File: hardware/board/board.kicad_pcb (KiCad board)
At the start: 4 copper layers, 300 x 120 mm, 235 parts, among them J201 LineOut, J202 Headphone, J203 LineIn, J301 MidiIn, J302 MidiOut, J501 USB_B_Micro, J502 USB_C_Receptacle_PowerOnly_6P, P501 USB_C_Plug_USB2.0, SW401 SW_Push, SW402 SW_Push, SW403 SW_Push, SW404 SW_Push, SW405 SW_Push, SW406 SW_Push, SW407 SW_Push, SW408 SW_Push, SW409 SW_Push, SW410 SW_Push, SW411 SW_Push, SW412 SW_Push, SW413 SW_Push, SW414 SW_Push, SW415 SW_Push, SW416 SW_Push, SW417 SW_Push, SW418 SW_Push, SW419 SW_Push, SW420 SW_Push, SW421 SW_Push, SW422 SW_Push, SW423 SW_Push, SW424 SW_Push, SW425 SW_Push, SW426 SW_Push, SW427 SW_Push, SW428 SW_Push, SW429 SW_Push, SW430 SW_Push, SW431 SW_Push, SW432 SW_Push, SW433 SW_Push, SW434 SW_Push, SW435 SW_Push, SW436 SW_Push, SW437 SW_Push, SW438 SW_Push, SW439 SW_Push, SW440 SW_Push, SW441 SW_Push, U101 Oled, U201 QFN40P700X700X80-57N, U202 TPS7A20xxxDBV, U301 RP2350_80QFN, U302 CNK_THB001P, U303 TLP2310, U304 74AHC1G125DCKR, U501 AP22653W6, U502 FSUSB42MX, U503 TPS259531DSGR, Y201 12.288MHz, Y301 ABM8-272-T3

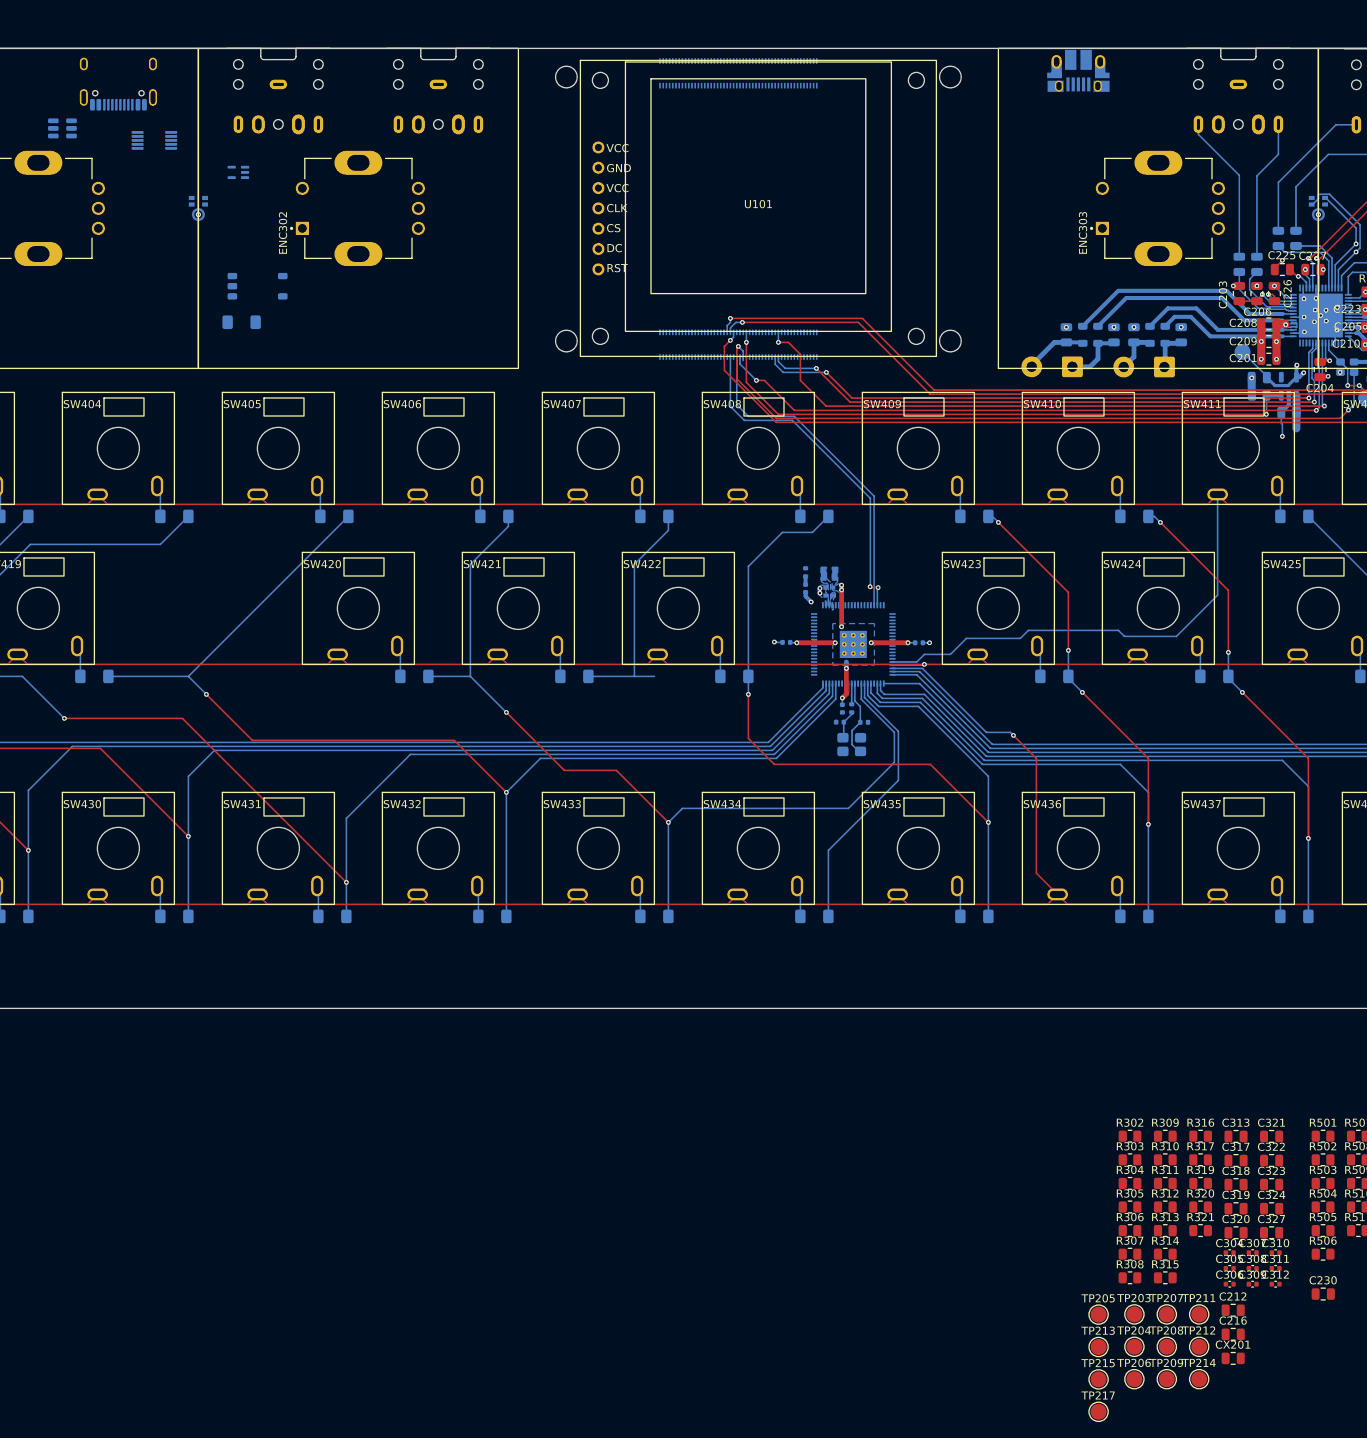
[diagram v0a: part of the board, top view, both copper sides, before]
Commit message: caps for 2350
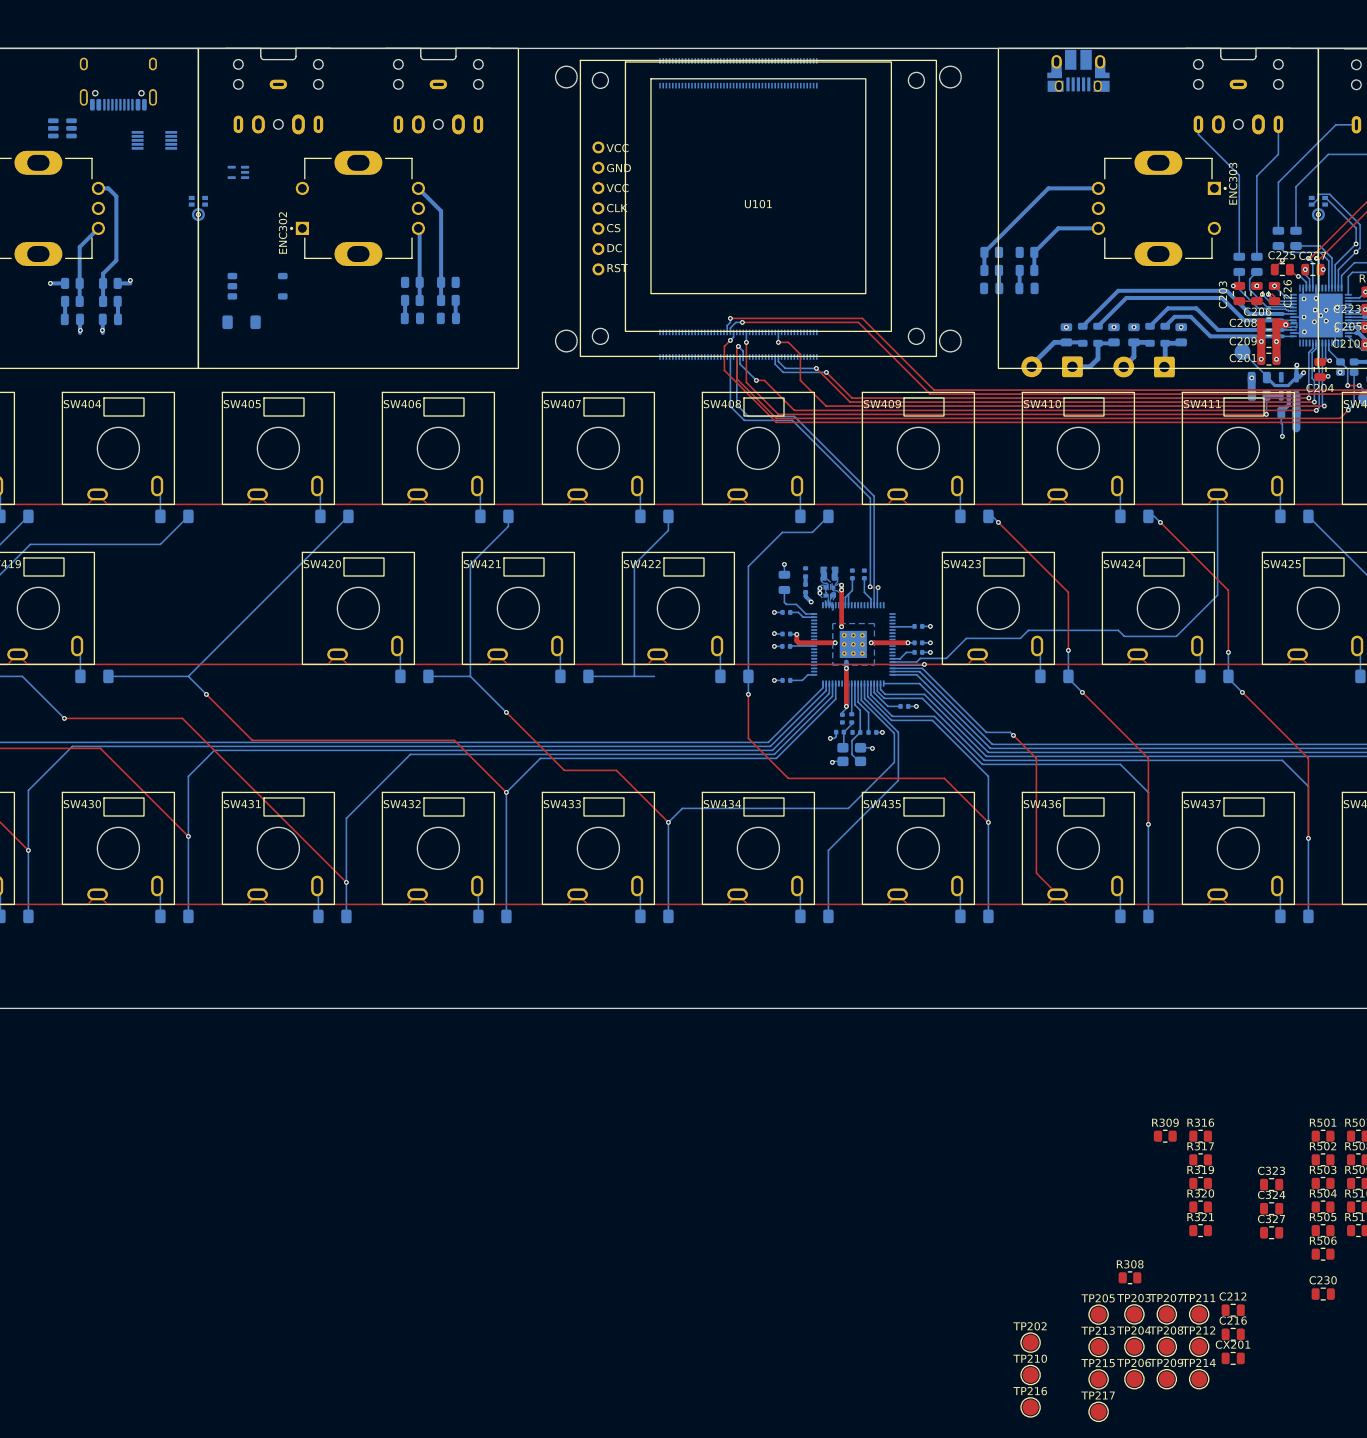
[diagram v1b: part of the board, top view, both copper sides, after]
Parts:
- added TP202: SPKLP, TestPoint:TestPoint_Pad_D2.0mm, F.Cu at (251.5, 245.3)
- added TP210: SPKRP, TestPoint:TestPoint_Pad_D2.0mm, F.Cu at (251.5, 249.3)
- added TP216: SPKRN, TestPoint:TestPoint_Pad_D2.0mm, F.Cu at (251.5, 253.4)
- C304, C305, C306, C307, C308, C309, C310, C311, C312, C313, C317, C318, C319, C320, C321, C322, R302, R303, R304, R305, R306, R307, R310, R311, R312, R313, R314, R315: moved to B.Cu
- U201: value QFN40P700X700X80-57N -> MAX98089ETN_T
- U302: value CNK_THB001P -> THB001P
- moved C317 179.5 mm to (131.8, 117.4)
- moved C318 177.5 mm to (136.5, 117.4), turned to 180 degrees
- moved R310 173.7 mm to (131.8, 115.1), turned to 180 degrees
- moved R311 171.9 mm to (136.5, 115.1)
- moved R302 169.8 mm to (131.8, 112.9)
- moved R303 168.1 mm to (136.5, 112.9), turned to 180 degrees
- moved C319 151.6 mm to (174.2, 117.2)
- moved C320 150.9 mm to (178.8, 117.2), turned to 180 degrees
- moved R312 147.3 mm to (174.2, 115.0), turned to 180 degrees
- moved R313 146.8 mm to (178.8, 115.0)
- moved R304 144.0 mm to (174.2, 112.8)
- moved R305 143.6 mm to (178.8, 112.8), turned to 180 degrees
- moved R315 127.1 mm to (251.1, 111.2), turned to 180 degrees
- moved R307 125.9 mm to (251.1, 109.0)
- moved R314 124.9 mm to (246.7, 111.2)
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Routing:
- net +3V3: track 12.1 -> 57.4 mm, vias 4 -> 6
- net Net-(ENC303-PadA): track 0.00 -> 19.8 mm
- net Net-(ENC301-PadB): track 0.00 -> 16.5 mm
- net GND: track 94.9 -> 111.1 mm, vias 38 -> 51
- net Net-(ENC302-PadB): track 0.00 -> 15.2 mm
- net Net-(ENC303-PadB): track 0.00 -> 11.5 mm
- net Net-(ENC301-PadA): track 0.00 -> 10.1 mm
- net Net-(ENC302-PadA): track 0.00 -> 9.07 mm
- net +1V1: track 28.5 -> 32.2 mm
- net /mcu/ENC1_B: track 0.00 -> 2.32 mm
- net /mcu/ENC3_A: track 0.00 -> 2.27 mm
- net /mcu/ENC3_B: track 0.00 -> 2.27 mm
- net /mcu/ENC2_B: track 0.00 -> 2.27 mm
- net /mcu/ENC2_A: track 0.00 -> 2.27 mm
- net /mcu/ENC1_A: track 0.00 -> 2.27 mm
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
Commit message: big routing board
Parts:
- added J101: UART, Connector_PinHeader_1.27mm:PinHeader_1x03_P1.27mm_Vertical, F.Cu at (234.6, 228.9)
- added J102: CM4_DEBUG, Connector_PinHeader_1.27mm:PinHeader_1x03_P1.27mm_Vertical, F.Cu at (238.7, 228.9)
- added J103: DEBUG_PORT, Connector_PinHeader_1.27mm:PinHeader_1x03_P1.27mm_Vertical, F.Cu at (242.9, 228.9)
- C323, C324, C327, R308, R309, R316, R317, R319, R320, R321: moved to B.Cu
- moved C327 180.3 mm to (157.5, 100.8), turned to -90 degrees
- moved R321 179.7 mm to (152.8, 97.5), turned to 180 degrees
- moved R320 174.9 mm to (156.8, 97.5), turned to 180 degrees
- moved R319 157.6 mm to (178.8, 98.8), turned to -90 degrees
- moved R308 133.2 mm to (314.0, 113.8), turned to 180 degrees
- moved R309 117.0 mm to (318.5, 113.8)
- moved C324 116.3 mm to (318.6, 118.2)
- moved R317 115.8 mm to (318.5, 116.0), turned to 180 degrees
- moved C323 112.0 mm to (314.0, 118.2), turned to 180 degrees
- moved R316 111.4 mm to (314.0, 116.0)
- moved U502 111.2 mm to (253.2, 92.8)
- moved D301 36.3 mm to (183.5, 98.2), turned to 0 degrees
- moved U303 30.0 mm to (183.5, 104.2), turned to -90 degrees
- moved U304 2.34 mm to (154.2, 100.7), turned to 90 degrees
- moved R302 0.15 mm to (131.8, 113.0), turned to 180 degrees
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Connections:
- U301 pad 3: /mcu/ENC1_A -> /mcu/ENC3_A
- U301 pad 4: /mcu/ENC1_B -> /mcu/ENC3_B
- U301 pad 42: unconnected-(U301-GPIO33-Pad42) -> /mcu/ENC1_SW
- U301 pad 43: /mcu/ENC3_A -> /mcu/ENC2_SW
- U301 pad 44: /mcu/ENC3_B -> /mcu/ENC1_A
- U301 pad 45: /mcu/ENC4_A -> /mcu/ENC1_B
- U301 pad 46: /mcu/ENC4_B -> /mcu/ENC2_A
- U301 pad 47: /mcu/ENC3_SW -> /mcu/ENC2_B
- U301 pad 48: /mcu/ENC4_SW -> unconnected-(U301-GPIO39-Pad48)
- U301 pad 52: unconnected-(U301-GPIO41_ADC1-Pad52) -> /mcu/JOYSTICK_X
- U301 pad 53: unconnected-(U301-GPIO42_ADC2-Pad53) -> /mcu/JOYSTICK_Y
- U301 pad 56: /mcu/JOYSTICK_X -> unconnected-(U301-GPIO45_ADC5-Pad56)
- U301 pad 57: /mcu/JOYSTICK_Y -> unconnected-(U301-GPIO46_ADC6-Pad57)
- U301 pad 6: /mcu/ENC2_A -> /mcu/ENC4_A
- U301 pad 7: /mcu/ENC2_B -> /mcu/ENC4_B
- U301 pad 79: /mcu/ENC1_SW -> /mcu/ENC3_SW
- U301 pad 80: /mcu/ENC2_SW -> /mcu/ENC4_SW
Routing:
- net /audio/DIGMICCLK: track 17.5 -> 174.0 mm, vias 1 -> 3
- net /audio/DIGMICDATA: track 14.0 -> 167.7 mm, vias 1 -> 3
- net /mcu/ENC1_SW: track 0.00 -> 140.4 mm
- net /mcu/ENC1_A: track 2.27 -> 115.4 mm
- net /mcu/ENC1_B: track 2.32 -> 111.8 mm
- net /mcu/ENC2_SW: track 0.00 -> 106.3 mm, vias 0 -> 2
- net /mcu/ENC4_B: track 0.00 -> 102.9 mm
- net /mcu/ENC4_A: track 0.00 -> 101.0 mm
- net /mcu/MIDI_RX: track 0.00 -> 93.4 mm
- net /mcu/ENC2_A: track 2.27 -> 75.5 mm
- net /mcu/ENC2_B: track 2.27 -> 72.1 mm
- net /mcu/ENC3_B: track 2.27 -> 53.6 mm
- net /mcu/ENC3_A: track 2.27 -> 51.5 mm
- net /mcu/MIDI_TX: track 0.00 -> 42.5 mm
- net /mcu/matrix_C6: track 64.5 -> 95.3 mm, vias 0 -> 4
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
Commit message: some big tim routing
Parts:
- C221: value 1uF -> 47pF
- C222: value 470pF -> 1uF
- C223: value 1uF -> 470pF
- C224: value 2.2uF -> 1uF
- C225: value 1uF -> 2.2uF
- C230: value 47pF -> 1uF
- C501, C502, C503, C504, C505, R501, R502, R503, R504, R505, R506, R507: moved to B.Cu
- J502: value USB_C_Receptacle_PowerOnly_6P -> USB_C_Receptacle_PowerOnly_24P
- R508: value 390k -> 5.1k; moved to B.Cu
- R509: value 681 @ 1% -> 5.1k; moved to B.Cu
- R510: value 5.1k -> 390k; moved to B.Cu
- R511: value 5.1k -> 681 @ 1%; moved to B.Cu
- moved C501 292.4 mm to (75.4, 28.7), turned to 180 degrees
- moved C502 292.4 mm to (75.4, 31.7), turned to 180 degrees
- moved R502 279.2 mm to (84.2, 31.6), turned to 180 degrees
- moved R504 279.2 mm to (84.2, 37.5), turned to 180 degrees
- moved C505 228.7 mm to (111.2, 98.0), turned to -90 degrees
- moved R510 226.0 mm to (110.8, 94.0), turned to 90 degrees
- moved R511 222.0 mm to (112.5, 101.2), turned to 180 degrees
- moved C504 220.6 mm to (116.8, 101.2)
- moved C503 220.3 mm to (117.2, 98.0), turned to -90 degrees
- moved R509 219.4 mm to (116.8, 94.0), turned to -90 degrees
- moved R507 219.0 mm to (113.0, 94.0), turned to -90 degrees
- moved R506 218.9 mm to (112.5, 103.5)
- moved R508 215.9 mm to (119.0, 94.0), turned to -90 degrees
- moved R503 197.2 mm to (139.8, 95.5), turned to 180 degrees
- moved R501 194.8 mm to (139.8, 93.2), turned to 180 degrees
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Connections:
- C221 pad 1: Net-(C221-Pad1) -> unconnected-(C221-Pad1)
- C221 pad 2: Net-(U201-INA2/EXTMICN) -> unconnected-(C221-Pad2)
- C222 pad 2: GND -> Net-(U201-INA2/EXTMICN)
- C223 pad 1: Net-(U201-REG) -> Net-(C223-Pad1)
- C224 pad 1: Net-(U201-REF) -> Net-(U201-REG)
- C225 pad 1: Net-(U201-HPVSS) -> Net-(U201-REF)
- C226 pad 1: /audio/C1N -> Net-(U201-HPVSS)
- C226 pad 2: /audio/C1P -> GND
- C227 pad 1: Net-(U201-HPVDD) -> /audio/C1N
- C227 pad 2: GND -> /audio/C1P
- C228 pad 1: +3V3 -> Net-(U201-HPVDD)
- C229 pad 1: +1V8 -> +3V3
- C230 pad 1: unconnected-(C230-Pad1) -> +1V8
- C230 pad 2: unconnected-(C230-Pad2) -> GND
- FB205 pad 2: Net-(C222-Pad1) -> Net-(C223-Pad1)
- J203 pad R: Net-(C221-Pad1) -> Net-(C222-Pad1)
- J502 pad A1: (no net) -> GND
- J502 pad A4: (no net) -> Net-(C503-Pad1)
- J502 pad B1: (no net) -> GND
- J502 pad B4: (no net) -> Net-(C503-Pad1)
- LS202 pad 1: Net-(C222-Pad1) -> Net-(C223-Pad1)
- R508 pad 1: Net-(U503-EN/UVLO) -> Net-(J502-CC2)
- R509 pad 1: /mcu/FUSE_ILM -> Net-(J502-CC1)
- R510 pad 1: Net-(J502-CC2) -> Net-(U503-EN/UVLO)
- R511 pad 1: Net-(J502-CC1) -> /mcu/FUSE_ILM
- TP216 pad 1: Net-(C222-Pad1) -> Net-(C223-Pad1)
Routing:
- net GND: track 122.9 -> 202.1 mm, vias 55 -> 75
- net /mcu/MIDI_TX: track 42.5 -> 66.6 mm, vias 0 -> 2
- net Net-(C503-Pad1): track 0.00 -> 20.2 mm, vias 0 -> 2
- net Net-(C222-Pad1): track 5.21 -> 24.0 mm
- net Net-(C221-Pad1): track 18.8 -> 0.00 mm
- net /usb/FUSE_~{FLT}: track 0.00 -> 4.97 mm
- net Net-(U503-EN/UVLO): track 0.00 -> 4.77 mm
- net Net-(J301-PadR): track 8.29 -> 12.0 mm
- net Net-(J302-PadR): track 7.52 -> 4.19 mm
- net Net-(J502-CC1): track 0.00 -> 2.75 mm
- net Net-(J502-CC2): track 0.00 -> 2.65 mm
- net +5V: track 10.2 -> 12.8 mm
- net /mcu/FUSE_ILM: track 0.00 -> 2.51 mm
- net /mcu/ENC1_SW: track 140.4 -> 137.9 mm
- net Net-(D301-K): track 3.62 -> 6.10 mm
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- added copper zone on B.Cu, net Net-(C503-Pad1)

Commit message: usb
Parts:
- added C102: 22uF X5R 16V, Capacitor_SMD:C_1206_3216Metric, B.Cu at (206.0, 125.2)
- added C103: 22uF X5R 16V, Capacitor_SMD:C_1206_3216Metric, B.Cu at (208.8, 125.2)
- C101: value 47uF -> 22uF X5R 16V; footprint Capacitor_SMD:C_0805_2012Metric -> Capacitor_SMD:C_1206_3216Metric; moved to B.Cu
- moved C101 136.9 mm to (211.5, 125.2), turned to -90 degrees
- moved C501 100.8 mm to (141.2, 105.0)
- moved C502 96.9 mm to (141.2, 102.8)
- moved R502 85.2 mm to (140.2, 95.8)
- moved R504 82.0 mm to (138.2, 99.2), turned to 90 degrees
- moved R505 13.6 mm to (162.4, 90.8), turned to 0 degrees
- moved R503 11.8 mm to (128.0, 94.0), turned to -90 degrees
- moved U501 9.85 mm to (141.2, 99.2), turned to 90 degrees
- moved U502 9.58 mm to (162.4, 93.8), turned to 180 degrees
- moved R501 9.53 mm to (130.2, 94.0), turned to 90 degrees
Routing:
- net +5V: track 12.8 -> 127.6 mm, vias 3 -> 17
- net /USB2_N: track 0.00 -> 63.1 mm
- net /USB2_P: track 0.00 -> 62.3 mm
- net Net-(P501-D+): track 0.00 -> 26.4 mm, vias 0 -> 2
- net Net-(P501-D-): track 0.00 -> 25.4 mm
- net GND: track 202.1 -> 224.8 mm, vias 75 -> 81
- net Net-(P501-VCONN): track 0.00 -> 17.2 mm
- net Net-(P501-CC): track 0.00 -> 11.7 mm
- net Net-(U501-OUT): track 0.00 -> 8.65 mm, vias 0 -> 2
- net Net-(J501-D-): track 0.00 -> 8.54 mm
- net Net-(J501-VBUS): track 0.00 -> 8.33 mm, vias 0 -> 2
- net Net-(J501-D+): track 0.00 -> 7.48 mm
- net /USB2_OTG_ID: track 0.00 -> 5.64 mm
- net Net-(U501-IN): track 0.00 -> 4.61 mm
- net Net-(U501-ILIM): track 0.00 -> 2.40 mm
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- added copper zone on In2.Cu, net GND
- removed copper zone on In1.Cu, net GND

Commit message: forgot input to ILIM
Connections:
- C501 pad 1: Net-(U501-IN) -> +5V
- C502 pad 1: Net-(U501-IN) -> +5V
- U501 pad 1: Net-(U501-IN) -> +5V
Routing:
- net +5V: track 127.6 -> 159.8 mm, vias 17 -> 20
- net Net-(U501-IN): track 4.61 -> 0.00 mm

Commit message: pre accidentally messed up the references
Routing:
- net +1V8: track 29.5 -> 193.4 mm, vias 5 -> 8
- net GND: track 224.8 -> 230.8 mm, vias 81 -> 83
- net /audio/DIGMICCLK: track 174.0 -> 175.3 mm, vias 3 -> 2
- net /audio/DIGMICDATA: track 167.7 -> 168.5 mm, vias 3 -> 2

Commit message: fix audio refs and also move almost every component to bottom layer
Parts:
- removed C230: 1uF, Capacitor_SMD:C_0805_2012Metric
- removed TP201: CODEC_MCLK, TestPoint:TestPoint_Pad_D2.0mm
- C201, C203, C204, C205, C206, C207, C210, C226, C227, CX201, R201, R202: moved to B.Cu
- C221: value 47pF -> 1uF
- C222: value 1uF -> 470pF
- C223: value 470pF -> 1uF; moved to B.Cu
- C224: value 1uF -> 2.2uF; moved to B.Cu
- C225: value 2.2uF -> 1uF; moved to B.Cu
- R508: value 5.1k -> 390k
- R509: value 5.1k -> 681 @ 1%
- R510: value 390k -> 5.1k
- R511: value 681 @ 1% -> 5.1k
- moved CX201 135.1 mm to (294.2, 113.2), turned to 180 degrees
- moved C321 4.25 mm to (246.7, 109.2)
- moved C322 4.25 mm to (251.1, 109.2)
- moved R306 4.25 mm to (246.7, 104.8)
- moved R307 4.25 mm to (251.1, 104.8)
- moved R314 4.25 mm to (246.7, 107.0)
- moved R315 4.25 mm to (251.1, 107.0)
- moved R202 3.75 mm to (298.0, 113.2)
- moved FB201 2.54 mm to (294.5, 126.2), turned to 0 degrees
- moved C202 1.79 mm to (294.5, 124.2), turned to 180 degrees
- moved C228 1.64 mm to (282.2, 129.0)
- moved C229 1.64 mm to (278.5, 124.6)
- moved R203 1.64 mm to (278.5, 126.8)
- moved TP218 1.64 mm to (276.4, 121.4)
- moved U202 1.64 mm to (282.2, 125.7)
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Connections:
- C221 pad 1: unconnected-(C221-Pad1) -> Net-(C221-Pad1)
- C221 pad 2: unconnected-(C221-Pad2) -> Net-(U201-INA2/EXTMICN)
- C222 pad 2: Net-(U201-INA2/EXTMICN) -> GND
- C223 pad 1: Net-(C223-Pad1) -> Net-(U201-REG)
- C224 pad 1: Net-(U201-REG) -> Net-(U201-REF)
- C225 pad 1: Net-(U201-REF) -> Net-(U201-HPVSS)
- C226 pad 1: Net-(U201-HPVSS) -> /audio/C1N
- C226 pad 2: GND -> /audio/C1P
- C227 pad 1: /audio/C1N -> Net-(U201-HPVDD)
- C227 pad 2: /audio/C1P -> GND
- C228 pad 1: Net-(U201-HPVDD) -> +3V3
- C229 pad 1: +3V3 -> +1V8
- C501 pad 1: +5V -> Net-(U501-IN)
- C502 pad 1: +5V -> Net-(U501-IN)
- FB205 pad 2: Net-(C223-Pad1) -> Net-(C222-Pad1)
- J203 pad R: Net-(C222-Pad1) -> Net-(C221-Pad1)
- LS202 pad 1: Net-(C223-Pad1) -> Net-(C222-Pad1)
- R508 pad 1: Net-(J502-CC2) -> Net-(U503-EN/UVLO)
- R509 pad 1: Net-(J502-CC1) -> /mcu/FUSE_ILM
- R510 pad 1: Net-(U503-EN/UVLO) -> Net-(J502-CC2)
- R511 pad 1: /mcu/FUSE_ILM -> Net-(J502-CC1)
- TP216 pad 1: Net-(C223-Pad1) -> Net-(C222-Pad1)
- U501 pad 1: +5V -> Net-(U501-IN)
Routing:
- net +5V: track 159.8 -> 246.8 mm
- net Net-(C222-Pad1): track 24.0 -> 5.21 mm
- net Net-(C221-Pad1): track 0.00 -> 17.3 mm
- net GND: track 230.8 -> 241.7 mm, vias 83 -> 85
- net Net-(C215-Pad2): track 18.7 -> 8.48 mm
- net Net-(C213-Pad2): track 17.7 -> 7.55 mm
- net Net-(U201-RECP/LOUTL/RXINP): track 8.97 -> 15.9 mm
- net Net-(U201-MCLK): track 9.65 -> 2.82 mm, vias 2 -> 0
- net Net-(U201-RECN/LOUTR/RXINN): track 10.0 -> 16.5 mm
- net Net-(U201-MICBIAS): track 2.48 -> 8.78 mm, vias 1 -> 0
- net +3V3: track 61.6 -> 66.4 mm, vias 6 -> 5
- net /I2C1_SDA: track 102.0 -> 106.4 mm
- net /I2C1_SCL: track 103.1 -> 107.5 mm
- net /mcu/ENC3_B: track 53.6 -> 57.8 mm
- net /mcu/ENC3_A: track 51.5 -> 55.7 mm
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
